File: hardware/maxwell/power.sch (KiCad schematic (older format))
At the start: 32 parts, among them J18 Supercap, J7 Dynamo Input, J9 Battery, Q2 PSMN5R4-25YLD, Q3 NTR1P02T1, Q4 NTR1P02T1, Q5 NTR1P02T1, U10 MIC39102, U3 TPS2113, U8 TLP188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

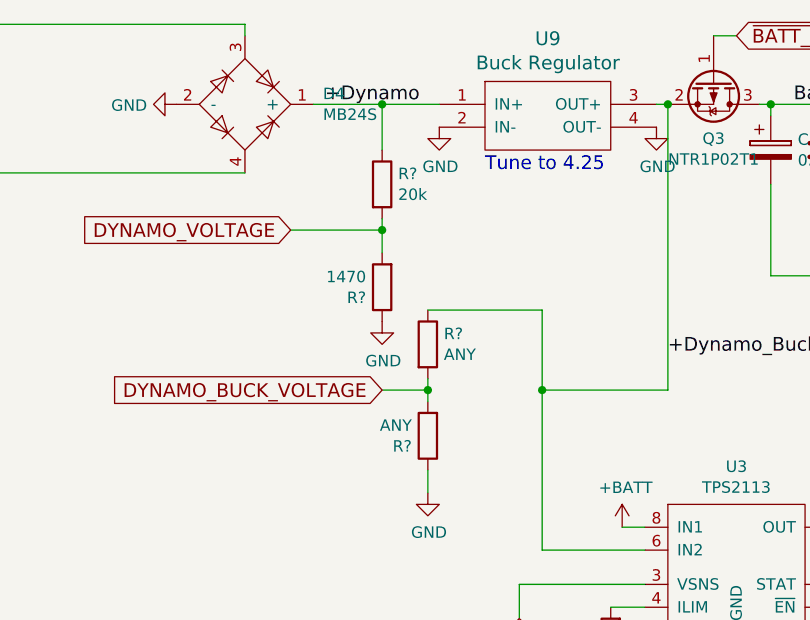
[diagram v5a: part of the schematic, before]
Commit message: Updating hardware to reference the proper libraries; adding new parts to board to support switching from dynamo input to battery.
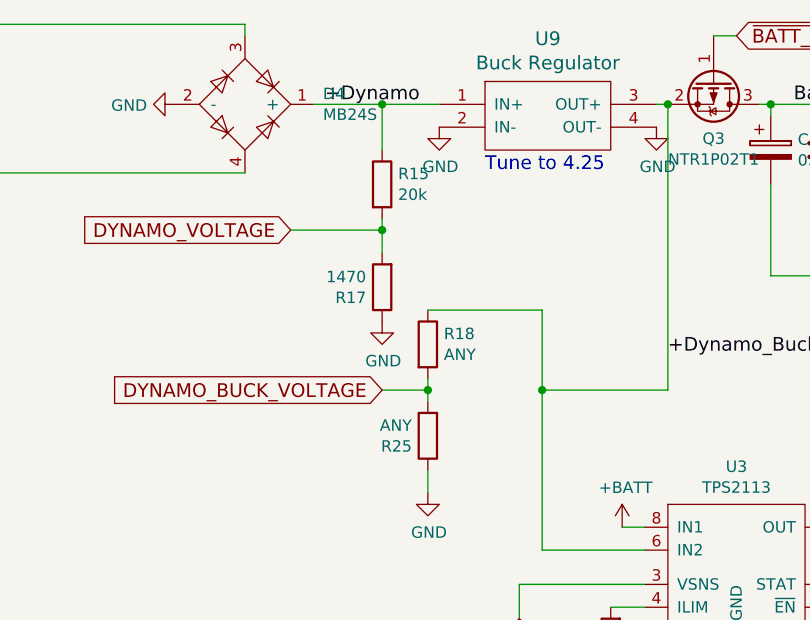
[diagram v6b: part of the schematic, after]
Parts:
- C17: footprint fruchti/fruchtilib/mod/rcl.pretty:CP_13mm_200 -> Capacitor_THT:CP_Radial_D13.0mm_P2.50mm
- C18, R12, R13, R14, R19, R20, R21, R22, R23, R24, R3: footprint coddingtonbear/coddingtonbear.pretty:0805_Milling -> coddingtonbear:0805_Milling
- D1: footprint mcous/kicad-lib/footprints/diode.pretty:DO-214AC -> coddingtonbear:DO-214AC
- D4: footprint coddingtonbear/coddingtonbear.pretty:SO-4_Milling -> coddingtonbear:SO-4_Milling
- J18, J7, J9: footprint coddingtonbear/coddingtonbear.pretty:JST_XH_B02B-XH-A_02x2.50mm_Straight_LargePads -> coddingtonbear:JST_XH_B02B-XH-A_02x2.50mm_Straight_LargePads
- Q2: footprint coddingtonbear/coddingtonbear.pretty:PSMN5R4-25YLD -> coddingtonbear:PSMN5R4-25YLD
- Q3, Q4, Q5: footprint coddingtonbear/coddingtonbear.pretty:SOT-23_LargePads -> coddingtonbear:SOT-23_LargePads
- R15, R17, R18, R25: renamed from R?; footprint coddingtonbear/coddingtonbear.pretty:0805_Milling -> coddingtonbear:0805_Milling
- U*1: footprint apexelectrix/apex-smd.pretty:SOT-23-5 -> Package_TO_SOT_SMD:SOT-23-5_HandSoldering
- U10: footprint adamgreig/agg-kicad/agg.pretty:SOIC-8 -> coddingtonbear:SOIC-8_3.9x4.9mm_P1.27mm_LargePads
- U8: footprint coddingtonbear/coddingtonbear.pretty:SO-4_Milling -> coddingtonbear:SO-4_Optocoupler_Milling
- U9: footprint coddingtonbear/coddingtonbear.pretty:BOOST_LM2596_3A -> coddingtonbear:BOOST_LM2596_3A
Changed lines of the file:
@@
 F 0 "J7" H 1579 1092 50  0000 L CNN
 F 1 "Dynamo Input" H 1579 1001 50  0000 L CNN
-F 2 "coddingtonbear/coddingtonbear.pretty:JST_XH_B02B-XH-A_02x2.50mm_Straight_LargePads" H 1500 1100 50  0001 C CNN
+F 2 "coddingtonbear:JST_XH_B02B-XH-A_02x2.50mm_Straight_LargePads" H 1500 1100 50  0001 C CNN
 F 3 "" H 1500 1100 50  0001 C CNN
 	1    1500 1100
@@
 F 0 "U8" H 1800 3025 50  0000 C CNN
 F 1 "TLP188" H 1800 2934 50  0000 C CNN
-F 2 "coddingtonbear/coddingtonbear.pretty:SO-4_Milling" H 1800 2400 50  0001 C CIN
+F 2 "coddingtonbear:SO-4_Optocoupler_Milling" H 1800 2400 50  0001 C CIN
 F 3 "" H 1800 2700 50  0001 L CNN
 	1    1800 2700
@@
 F 0 "D1" V 1546 3171 50  0000 R CNN
 F 1 "GS1M-LTP" V 1455 3171 50  0000 R CNN
-F 2 "mcous/kicad-lib/footprints/diode.pretty:DO-214AC" H 1500 3250 50  0001 C CNN
+F 2 "coddingtonbear:DO-214AC" H 1500 3250 50  0001 C CNN
 F 3 "" H 1500 3250 50  0001 C CNN
 	1    1500 3250
@@
 F 0 "D4" H 3691 1296 50  0000 L CNN
 F 1 "MB24S" H 3691 1205 50  0000 L CNN
-F 2 "coddingtonbear/coddingtonbear.pretty:SO-4_Milling" H 3350 1250 50  0001 C CNN
+F 2 "coddingtonbear:SO-4_Milling" H 3350 1250 50  0001 C CNN
 F 3 "" H 3350 1250 50  0001 C CNN
 	1    3350 1250
@@
 F 0 "R14" H 1570 2996 50  0000 L CNN
 F 1 "200" H 1570 2905 50  0000 L CNN
-F 2 "coddingtonbear/coddingtonbear.pretty:0805_Milling" V 1430 2950 50  0001 C CNN
+F 2 "coddingtonbear:0805_Milling" V 1430 2950 50  0001 C CNN
 F 3 "" H 1500 2950 50  0001 C CNN
 	1    1500 2950
@@
 F 0 "U9" H 4675 1637 60  0000 C CNN
 F 1 "Buck Regulator" H 4675 1531 60  0000 C CNN
-F 2 "coddingtonbear/coddingtonbear.pretty:BOOST_LM2596_3A" H 4700 1300 60  0001 C CNN
+F 2 "coddingtonbear:BOOST_LM2596_3A" H 4700 1300 60  0001 C CNN
 F 3 "" H 4700 1300 60  0001 C CNN
 	1    4700 1300
@@
 F 0 "U*1" H 6850 2197 60  0000 C CNN
 F 1 "MCP73831T" H 6850 2091 60  0000 C CNN
-F 2 "apexelectrix/apex-smd.pretty:SOT-23-5" H 6850 1300 60  0001 C CNN
+F 2 "Package_TO_SOT_SMD:SOT-23-5_HandSoldering" H 6850 1300 60  0001 C CNN
 F 3 "" H 6850 1300 60  0000 C CNN
 	1    6850 1600
@@
 F 0 "J9" H 8680 1242 50  0000 L CNN
 F 1 "Battery" H 8680 1151 50  0000 L CNN
-F 2 "coddingtonbear/coddingtonbear.pretty:JST_XH_B02B-XH-A_02x2.50mm_Straight_LargePads" H 8600 1250 50  0001 C CNN
+F 2 "coddingtonbear:JST_XH_B02B-XH-A_02x2.50mm_Straight_LargePads" H 8600 1250 50  0001 C CNN
 F 3 "" H 8600 1250 50  0001 C CNN
 	1    8600 1250
@@
 F 0 "R19" H 7520 1696 50  0000 L CNN
 F 1 "2k" H 7520 1605 50  0000 L CNN
-F 2 "coddingtonbear/coddingtonbear.pretty:0805_Milling" V 7380 1650 50  0001 C CNN
+F 2 "coddingtonbear:0805_Milling" V 7380 1650 50  0001 C CNN
 F 3 "" H 7450 1650 50  0001 C CNN
 	1    7450 1650
@@
 F 0 "C18" H 5785 1404 50  0000 R CNN
 F 1 "100nF" H 5785 1495 50  0000 R CNN
-F 2 "coddingtonbear/coddingtonbear.pretty:0805_Milling" H 5938 1300 50  0001 C CNN
+F 2 "coddingtonbear:0805_Milling" H 5938 1300 50  0001 C CNN
 F 3 "" H 5900 1450 50  0001 C CNN
 	1    5900 1450
@@
 F 0 "R20" H 9370 1996 50  0000 L CNN
 F 1 "ANY" H 9370 1905 50  0000 L CNN
-F 2 "coddingtonbear/coddingtonbear.pretty:0805_Milling" V 9230 1950 50  0001 C CNN
+F 2 "coddingtonbear:0805_Milling" V 9230 1950 50  0001 C CNN
 F 3 "" H 9300 1950 50  0001 C CNN
 	1    9300 1950
@@
 F 0 "R21" H 9370 2396 50  0000 L CNN
 F 1 "ANY" H 9370 2305 50  0000 L CNN
-F 2 "coddingtonbear/coddingtonbear.pretty:0805_Milling" V 9230 2350 50  0001 C CNN
+F 2 "coddingtonbear:0805_Milling" V 9230 2350 50  0001 C CNN
 F 3 "" H 9300 2350 50  0001 C CNN
 	1    9300 2350
@@
 F 0 "R23" H 10170 1996 50  0000 L CNN
 F 1 "ANY" H 10170 1905 50  0000 L CNN
-F 2 "coddingtonbear/coddingtonbear.pretty:0805_Milling" V 10030 1950 50  0001 C CNN
+F 2 "coddingtonbear:0805_Milling" V 10030 1950 50  0001 C CNN
 F 3 "" H 10100 1950 50  0001 C CNN
 	1    10100 1950
@@
 F 0 "R24" H 10170 2396 50  0000 L CNN
 F 1 "ANY" H 10170 2305 50  0000 L CNN
-F 2 "coddingtonbear/coddingtonbear.pretty:0805_Milling" V 10030 2350 50  0001 C CNN
+F 2 "coddingtonbear:0805_Milling" V 10030 2350 50  0001 C CNN
 F 3 "" H 10100 2350 50  0001 C CNN
 	1    10100 2350
@@
 F 0 "R22" V 9493 1100 50  0000 C CNN
 F 1 "0.02" V 9584 1100 50  0000 C CNN
-F 2 "coddingtonbear/coddingtonbear.pretty:0805_Milling" V 9630 1100 50  0001 C CNN
+F 2 "coddingtonbear:0805_Milling" V 9630 1100 50  0001 C CNN
 F 3 "" H 9700 1100 50  0001 C CNN
 	1    9700 1100
@@
 F 0 "C17" H 5768 1496 50  0000 L CNN
 F 1 "0.1" H 5768 1405 50  0000 L CNN
-F 2 "fruchti/fruchtilib/mod/rcl.pretty:CP_13mm_200" H 5688 1300 50  0001 C CNN
+F 2 "Capacitor_THT:CP_Radial_D13.0mm_P2.50mm" H 5688 1300 50  0001 C CNN
 F 3 "" H 5650 1450 50  0001 C CNN
 	1    5650 1450
@@
 F 0 "Q4" V 8193 1350 50  0000 C CNN
 F 1 "NTR1P02T1" V 8102 1350 50  0000 C CNN
-F 2 "coddingtonbear/coddingtonbear.pretty:SOT-23_LargePads" H 8050 1450 50  0001 C CNN
+F 2 "coddingtonbear:SOT-23_LargePads" H 8050 1450 50  0001 C CNN
 F 3 "" H 7850 1350 50  0001 C CNN
 	1    7850 1350
@@
 F 0 "Q3" V 5650 1150 50  0000 C CNN
 F 1 "NTR1P02T1" V 5741 1150 50  0000 C CNN
-F 2 "coddingtonbear/coddingtonbear.pretty:SOT-23_LargePads" H 5600 1250 50  0001 C CNN
+F 2 "coddingtonbear:SOT-23_LargePads" H 5600 1250 50  0001 C CNN
 F 3 "" H 5400 1150 50  0001 C CNN
 	1    5400 1150
@@
 F 0 "Q2" H 3356 3946 50  0000 L CNN
 F 1 "PSMN5R4-25YLD" H 3356 3855 50  0000 L CNN
-F 2 "coddingtonbear/coddingtonbear.pretty:PSMN5R4-25YLD" H 3350 4000 50  0001 C CNN
+F 2 "coddingtonbear:PSMN5R4-25YLD" H 3350 4000 50  0001 C CNN
 F 3 "" H 3150 3900 50  0001 C CNN
 	1    3150 3900
@@
 F 0 "U10" H 7925 3837 60  0000 C CNN
 F 1 "MIC39102" H 7925 3731 60  0000 C CNN
-F 2 "adamgreig/agg-kicad/agg.pretty:SOIC-8" H 7900 3350 60  0001 C CNN
+F 2 "coddingtonbear:SOIC-8_3.9x4.9mm_P1.27mm_LargePads" H 7900 3350 60  0001 C CNN
 F 3 "" H 7900 3350 60  0001 C CNN
 	1    7900 3350
@@
 F 0 "R12" V 7407 3500 50  0000 C CNN
 F 1 "16-17k" V 7316 3500 50  0000 C CNN
-F 2 "coddingtonbear/coddingtonbear.pretty:0805_Milling" V 7130 3500 50  0001 C CNN
+F 2 "coddingtonbear:0805_Milling" V 7130 3500 50  0001 C CNN
 F 3 "" H 7200 3500 50  0001 C CNN
 	1    7200 3500
@@
 F 0 "R13" V 7407 3800 50  0000 C CNN
 F 1 "10k" V 7316 3800 50  0000 C CNN
-F 2 "coddingtonbear/coddingtonbear.pretty:0805_Milling" V 7130 3800 50  0001 C CNN
+F 2 "coddingtonbear:0805_Milling" V 7130 3800 50  0001 C CNN
 F 3 "" H 7200 3800 50  0001 C CNN
 	1    7200 3800
@@
 F 0 "Q5" V 9543 1200 50  0000 C CNN
 F 1 "NTR1P02T1" V 9452 1200 50  0000 C CNN
-F 2 "coddingtonbear/coddingtonbear.pretty:SOT-23_LargePads" H 9400 1300 50  0001 C CNN
+F 2 "coddingtonbear:SOT-23_LargePads" H 9400 1300 50  0001 C CNN
 F 3 "" H 9200 1200 50  0001 C CNN
 	1    9200 1200
@@
 F 0 "J18" H 8080 4392 50  0000 L CNN
 F 1 "Supercap" H 8080 4301 50  0000 L CNN
-F 2 "coddingtonbear/coddingtonbear.pretty:JST_XH_B02B-XH-A_02x2.50mm_Straight_LargePads" H 8000 4400 50  0001 C CNN
+F 2 "coddingtonbear:JST_XH_B02B-XH-A_02x2.50mm_Straight_LargePads" H 8000 4400 50  0001 C CNN
 F 3 "" H 8000 4400 50  0001 C CNN
 	1    8000 4400
@@
 F 0 "R3" V 5157 3600 50  0000 C CNN
 F 1 "500" V 5066 3600 50  0000 C CNN
-F 2 "coddingtonbear/coddingtonbear.pretty:0805_Milling" V 4880 3600 50  0001 C CNN
+F 2 "coddingtonbear:0805_Milling" V 4880 3600 50  0001 C CNN
 F 3 "" H 4950 3600 50  0001 C CNN
 	1    4950 3600
@@
 DYNAMO_BUCK_VOLTAGE
 $Comp
-L maxwell-rescue:R-RESCUE-maxwell R?
+L maxwell-rescue:R-RESCUE-maxwell R18
 U 1 1 5BCDF6C1
 P 4150 2300
-F 0 "R?" H 4220 2346 50  0000 L CNN
+F 0 "R18" H 4220 2346 50  0000 L CNN
 F 1 "ANY" H 4220 2255 50  0000 L CNN
-F 2 "coddingtonbear/coddingtonbear.pretty:0805_Milling" V 4080 2300 50  0001 C CNN
+F 2 "coddingtonbear:0805_Milling" V 4080 2300 50  0001 C CNN
 F 3 "" H 4150 2300 50  0001 C CNN
 	1    4150 2300
@@
 Connection ~ 4650 2500
 $Comp
-L maxwell-rescue:R-RESCUE-maxwell R?
+L maxwell-rescue:R-RESCUE-maxwell R25
 U 1 1 5BCE1A8A
 P 4150 2700
-F 0 "R?" H 4220 2746 50  0000 L CNN
+F 0 "R25" H 4220 2746 50  0000 L CNN
 F 1 "ANY" H 4220 2655 50  0000 L CNN
-F 2 "coddingtonbear/coddingtonbear.pretty:0805_Milling" V 4080 2700 50  0001 C CNN
+F 2 "coddingtonbear:0805_Milling" V 4080 2700 50  0001 C CNN
 F 3 "" H 4150 2700 50  0001 C CNN
 	1    4150 2700
@@
 $EndComp
 $Comp
-L maxwell-rescue:GND-RESCUE-maxwell #PWR?
+L maxwell-rescue:GND-RESCUE-maxwell #PWR0114
 U 1 1 5BCE5FA3
 P 4150 2950
-F 0 "#PWR?" H 4150 2700 50  0001 C CNN
+F 0 "#PWR0114" H 4150 2700 50  0001 C CNN
 F 1 "GND" H 4155 2777 50  0000 C CNN
 F 2 "" H 4150 2950 50  0001 C CNN
@@
 	4150 2850 4150 2950
 $Comp
-L maxwell-rescue:R-RESCUE-maxwell R?
+L maxwell-rescue:R-RESCUE-maxwell R15
 U 1 1 5BCF3736
 P 3950 1600
-F 0 "R?" H 4020 1646 50  0000 L CNN
+F 0 "R15" H 4020 1646 50  0000 L CNN
 F 1 "20k" H 4020 1555 50  0000 L CNN
-F 2 "coddingtonbear/coddingtonbear.pretty:0805_Milling" V 3880 1600 50  0001 C CNN
+F 2 "coddingtonbear:0805_Milling" V 3880 1600 50  0001 C CNN
 F 3 "" H 3950 1600 50  0001 C CNN
 	1    3950 1600
@@
 $EndComp
 $Comp
-L maxwell-rescue:R-RESCUE-maxwell R?
+L maxwell-rescue:R-RESCUE-maxwell R17
 U 1 1 5BCF4E13
 P 3950 2050
-F 0 "R?" H 4020 2096 50  0000 L CNN
+F 0 "R17" H 4020 2096 50  0000 L CNN
 F 1 "1470" H 4020 2005 50  0000 L CNN
-F 2 "coddingtonbear/coddingtonbear.pretty:0805_Milling" V 3880 2050 50  0001 C CNN
+F 2 "coddingtonbear:0805_Milling" V 3880 2050 50  0001 C CNN
 F 3 "" H 3950 2050 50  0001 C CNN
 	1    3950 2050
@@
 $EndComp
 $Comp
-L maxwell-rescue:GND-RESCUE-maxwell #PWR?
+L maxwell-rescue:GND-RESCUE-maxwell #PWR0115
 U 1 1 5BCF74EA
 P 3950 2200
-F 0 "#PWR?" H 3950 1950 50  0001 C CNN
+F 0 "#PWR0115" H 3950 1950 50  0001 C CNN
 F 1 "GND" H 3955 2027 50  0000 C CNN
 F 2 "" H 3950 2200 50  0001 C CNN

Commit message: v1.5 ready for production.
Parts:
- removed J18: Supercap, coddingtonbear:JST_XH_B02B-XH-A_02x2.50mm_Straight_LargePads, symbol maxwell-rescue:Conn_01x02-RESCUE-maxwell
- removed Q3: NTR1P02T1, coddingtonbear:SOT-23_LargePads, symbol maxwell-rescue:Q_PMOS_GSD-device
- added C1, C15, C16: 0.1u, coddingtonbear:0805_Milling, symbol maxwell-rescue:C-RESCUE-maxwell
- added R11: 10k, coddingtonbear:0805_Milling, symbol maxwell-rescue:R-RESCUE-maxwell
- added R?: 250, coddingtonbear:0805_Milling, symbol maxwell-rescue:R-RESCUE-maxwell
- added U1: MCP1501, Package_TO_SOT_SMD:TSOT-23-6_HandSoldering, symbol maxwell-rescue:MCP1501-coddingtonbear
- added U11: SN74LVC1G14DBVR, Package_TO_SOT_SMD:SOT-23-5_HandSoldering, symbol digikey:SN74LVC1G14DBVR
- added U4: PCA9536D, coddingtonbear:SOIC-8_3.9x4.9mm_P1.27mm_LargePads, symbol Interface_Expansion:PCA9536D
- added U6: AD7995, Package_TO_SOT_SMD:SOT-23-8_Handsoldering, symbol coddingtonbear:AD7995
- C17: footprint Capacitor_THT:CP_Radial_D13.0mm_P2.50mm -> coddingtonbear:JST_XH_B02B-XH-A_02x2.50mm_Straight_LargePads
- R18: value ANY -> 2k
- R25: value ANY -> 1k
- R3: value 500 -> 10k
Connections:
- net Batt_Charge is gone; now on net +Dynamo_Buck: C17.1, C18.2, U*1.4 (VDD)
- net +3V3: now also C1.1, C15.2, C16.2, R11.2, U1.6 (VDD), U4.8 (VDD), U6.8 (VDD)
- net +BATT: now also U3.6 (IN2), U11.5 (VCC); no longer U3.8 (IN1)
- net +Dynamo_Buck: now also U3.8 (IN1); no longer R18.1, U3.6 (IN2)
- net BATT_VOLTAGE: now also U6.4 (VIN1)
- net CURRENT_SENSE: now also U6.3 (VIN0)
- net DYNAMO_VOLTAGE: now also U6.5 (VIN3)
- net GND: now also R25.2, C1.2, C15.1, C16.1, R?.1, U1.2 (GND), U1.3 (GND), U1.5 (GND), U11.3 (GND), U4.4 (VSS), U6.7 (GND); no longer R25.1, R3.1
- net ~BATT_CHARGING: now also U4.3 (IO2)
- net BATT_CHARGE_PRE_POLARITY: now reaches Q4.3 (D), U*1.3 (VBAT)
- net BATT_PRE_POLARITY: now reaches J9.2 (Pin_2), Q4.2 (S), Q5.3 (D)
- net BATT_PRE_SENSE: now reaches Q5.2 (S), R20.1, R22.2
- net BATT_PRE_SENSE: now also R18.1
- net POWER_SOURCE_INDICATOR: now reaches U3.1 (STAT)
- net POWER_SOURCE_INDICATOR: now also U4.2 (IO1)
- net at U3.4 (ILIM): now also R?.2; no longer R3.2
- net DYNAMO_BUCK_VOLTAGE renamed ~BATT_DISABLE
- net ~BATT_DISABLE: now also R25.1, U11.2 (A); no longer R25.2
- net DYNAMO_SOURCE_DISABLE renamed BATTERY_SOURCE_DISABLE
- net BATTERY_SOURCE_DISABLE: now also R3.1, U4.1 (IO0)
- new net: R3.2, U11.4 (Y)
- new net: U1.1 (OUT), U6.6 (VIN4/VREF)
- new net ENABLE_VREF: R11.1, U1.4 (~SHDN), U4.5 (IO3)
- new net I2C1_SCL: U4.6 (SCL), U6.1 (SCL)
- new net I2C1_SDA: U4.7 (SDA), U6.2 (SDA)
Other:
- note added: "Addr: 0101000\n"
- note added: "Addr: 1000001\n"
- moved on the sheet: Q2, R3

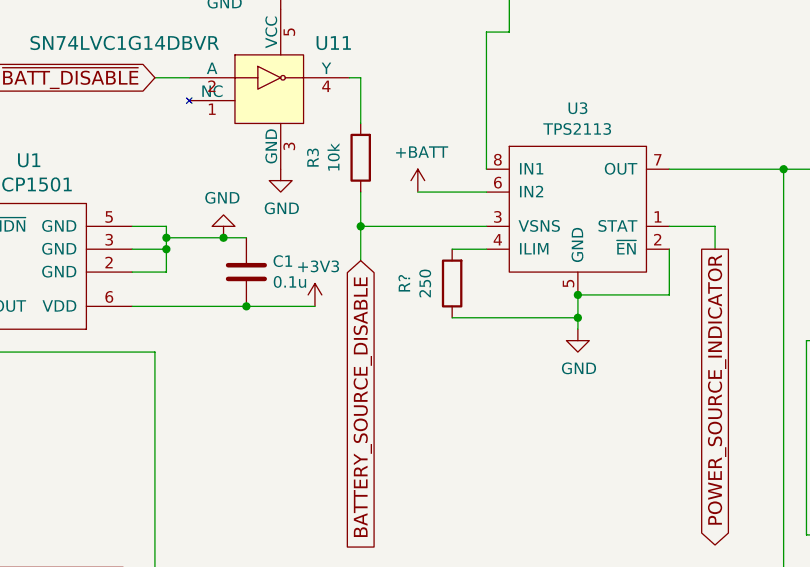
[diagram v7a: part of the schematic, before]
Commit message: Minor updates to mak certain pads slightly larger.
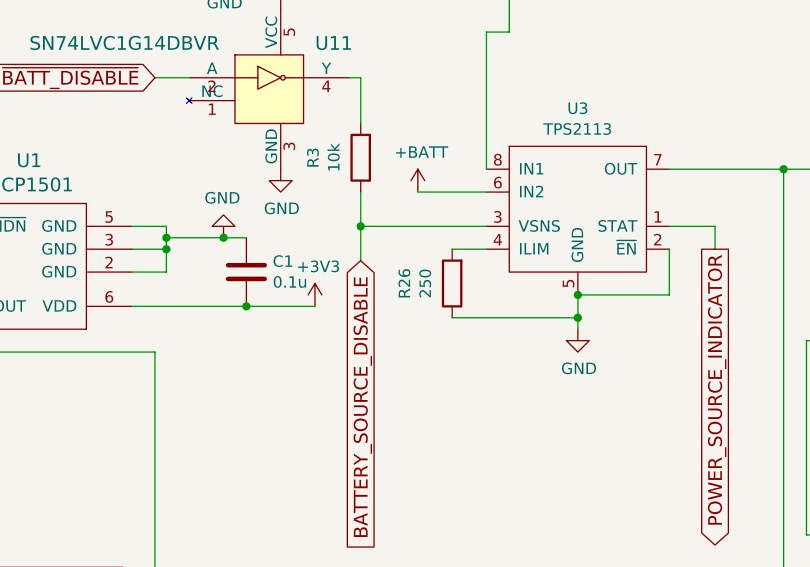
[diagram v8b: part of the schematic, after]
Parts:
- gave numbers to parts that had none: 1
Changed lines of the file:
@@
 	3800 2700 3650 2700
 $Comp
-L maxwell-rescue:R-RESCUE-maxwell R?
+L maxwell-rescue:R-RESCUE-maxwell R26
 U 1 1 5C04CF20
 P 4950 3600
-F 0 "R?" V 5157 3600 50  0000 C CNN
+F 0 "R26" V 5157 3600 50  0000 C CNN
 F 1 "250" V 5066 3600 50  0000 C CNN
 F 2 "coddingtonbear:0805_Milling" V 4880 3600 50  0001 C CNN
